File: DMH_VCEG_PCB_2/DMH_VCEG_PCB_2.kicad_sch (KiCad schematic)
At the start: 0 parts

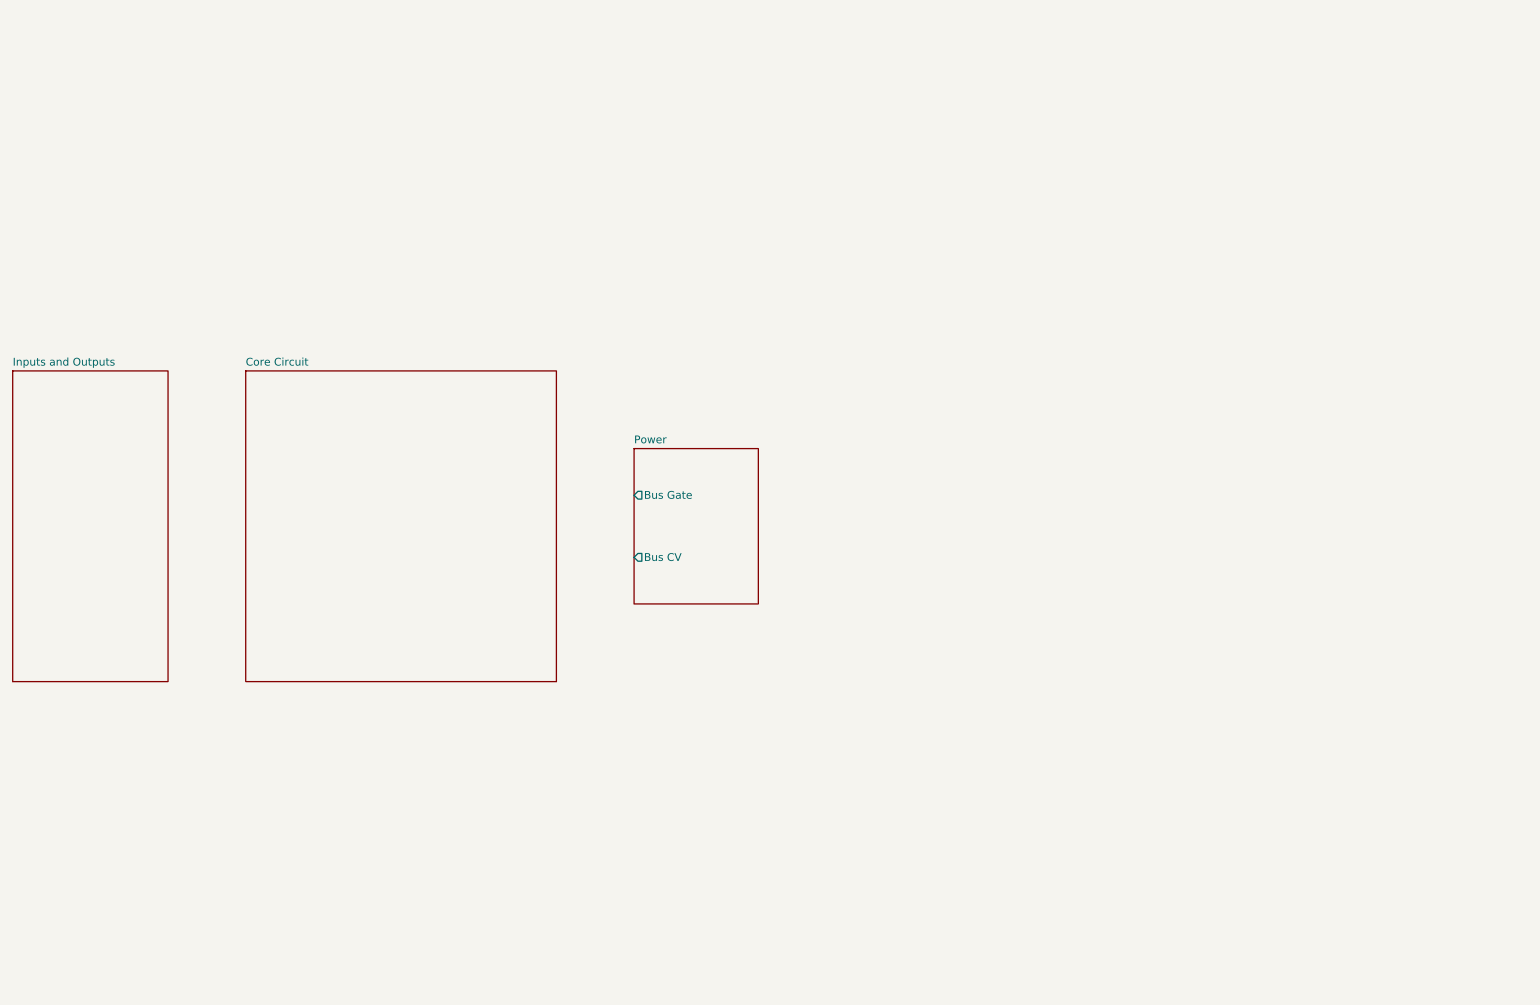
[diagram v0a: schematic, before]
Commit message: Copied PCB 1 as PCB 2
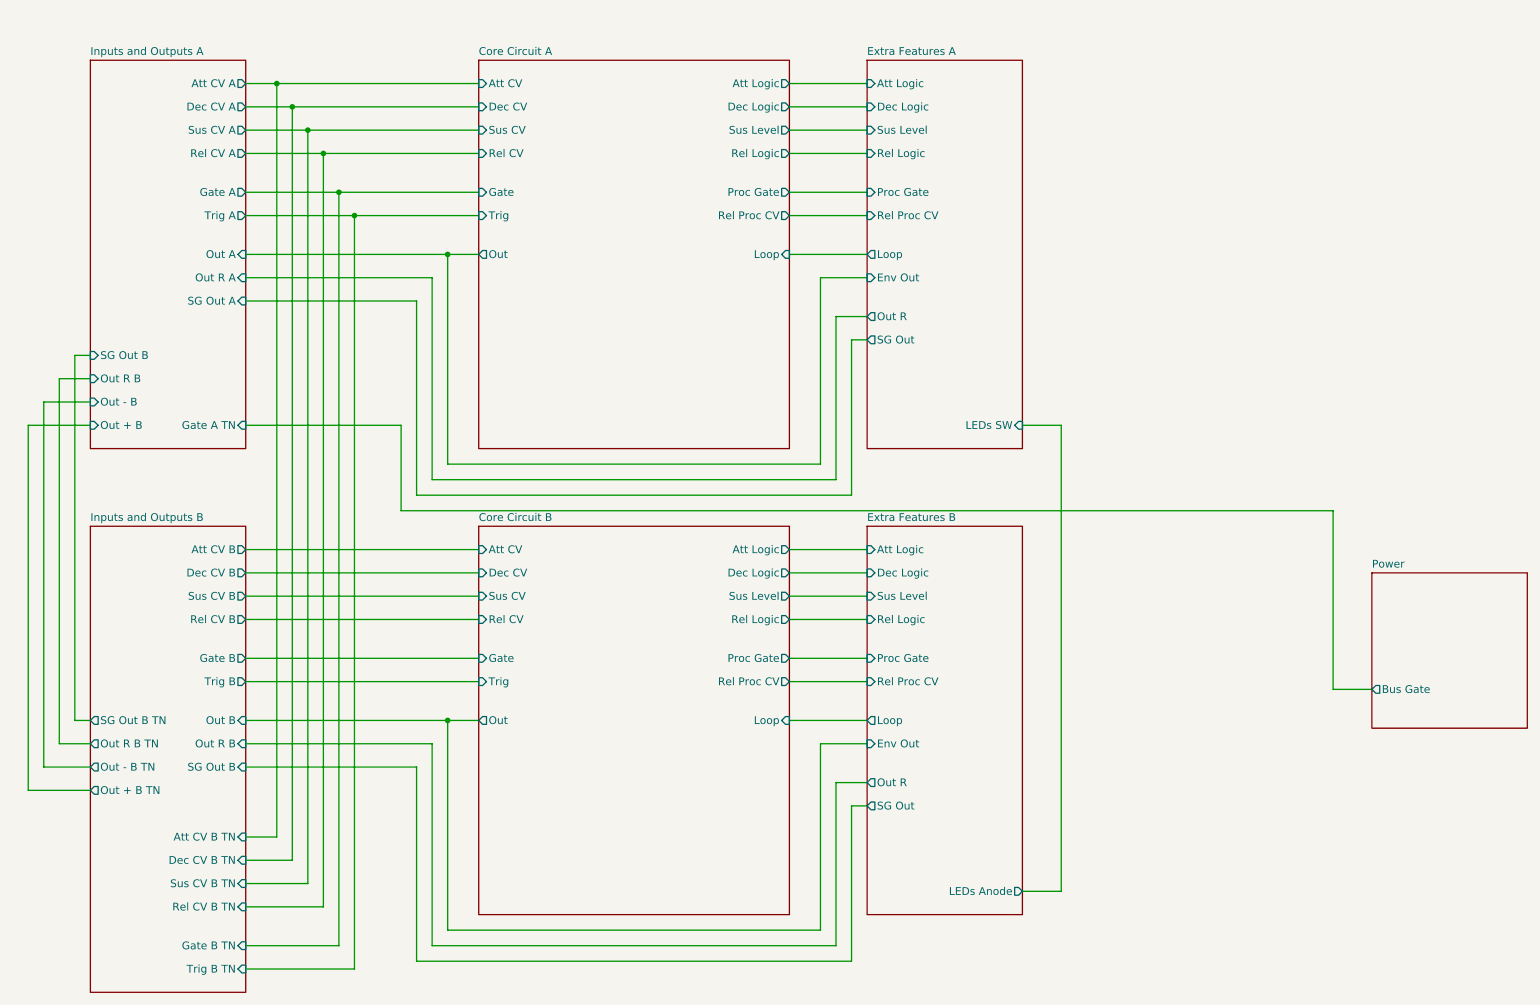
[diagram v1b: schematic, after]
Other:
- sheet Inputs and Outputs renamed Inputs and Outputs A
- removed sheet Core Circuit
- added sheet Core Circuit A (Core_Circuit_A.kicad_sch)
- added sheet Core Circuit B (Core_Circuit_B.kicad_sch)
- added sheet Extra Features A (Extra_Features_A.kicad_sch)
- added sheet Extra Features B (Extra_Features_B.kicad_sch)
- added sheet Inputs and Outputs B (Inputs_and_Outputs_B.kicad_sch)
- sheet Inputs and Outputs A: file Inputs_and_Outputs.kicad_sch -> Inputs_and_Outputs_A.kicad_sch
- sheet Inputs and Outputs A ports: added Att CV A, Dec CV A, Gate A, Gate A TN, Out + B, Out - B, Out A, Out R A, Out R B, Rel CV A, SG Out A, SG Out B, Sus CV A, Trig A; removed none
- sheet Power ports: added none; removed Bus CV

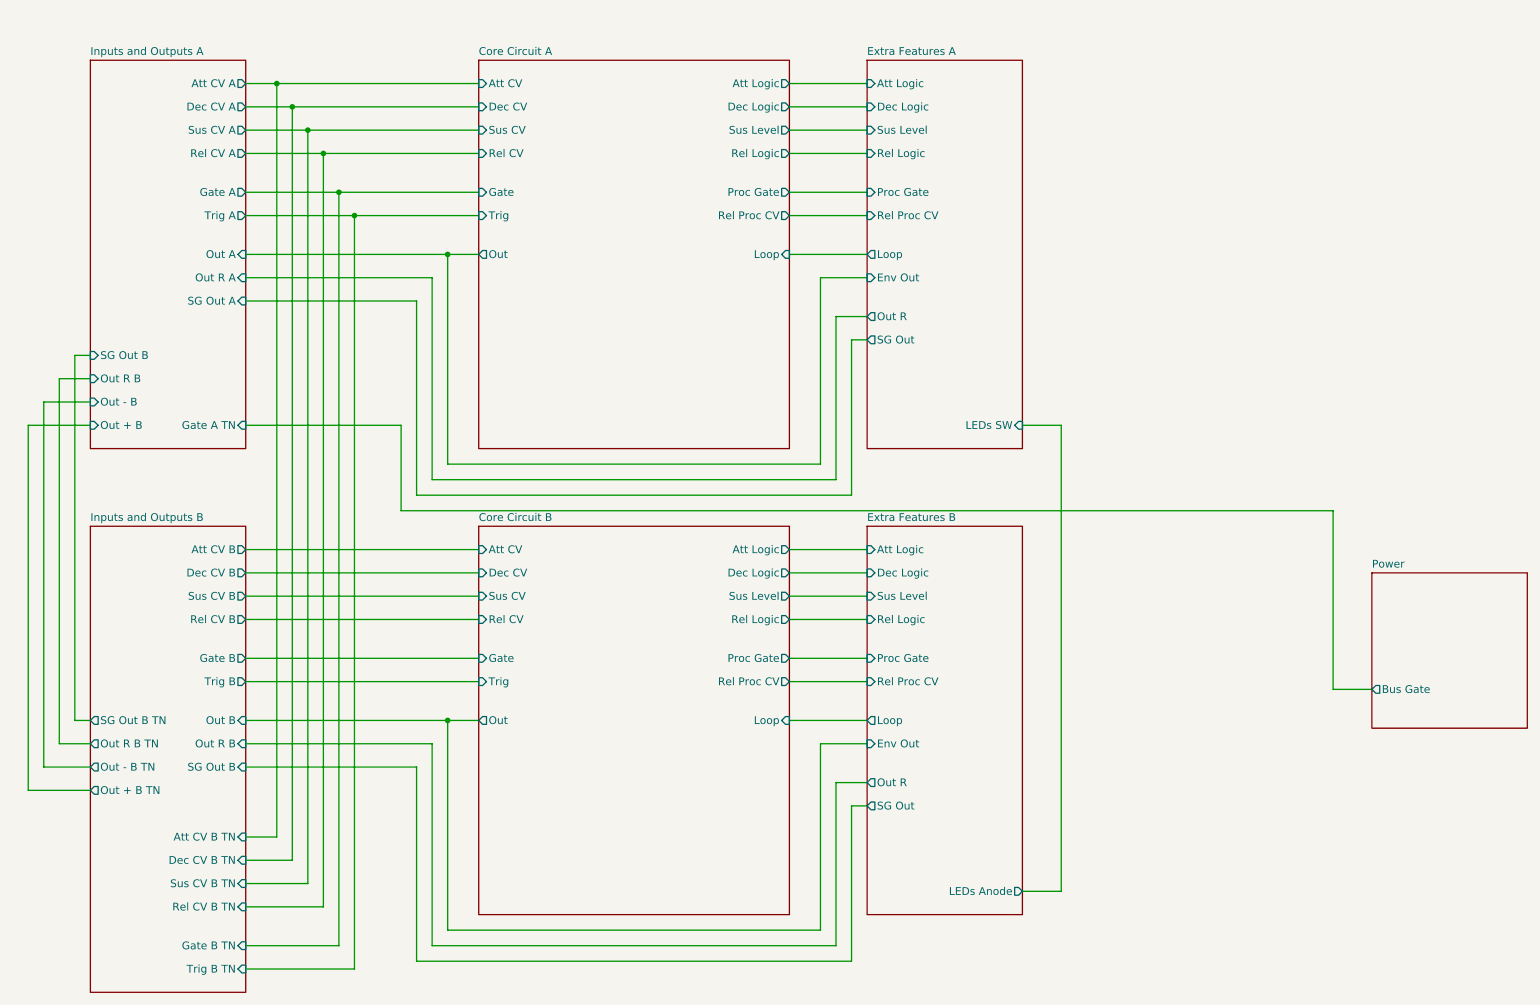
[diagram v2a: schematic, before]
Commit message: Synced PCB 2 project with PCB 1
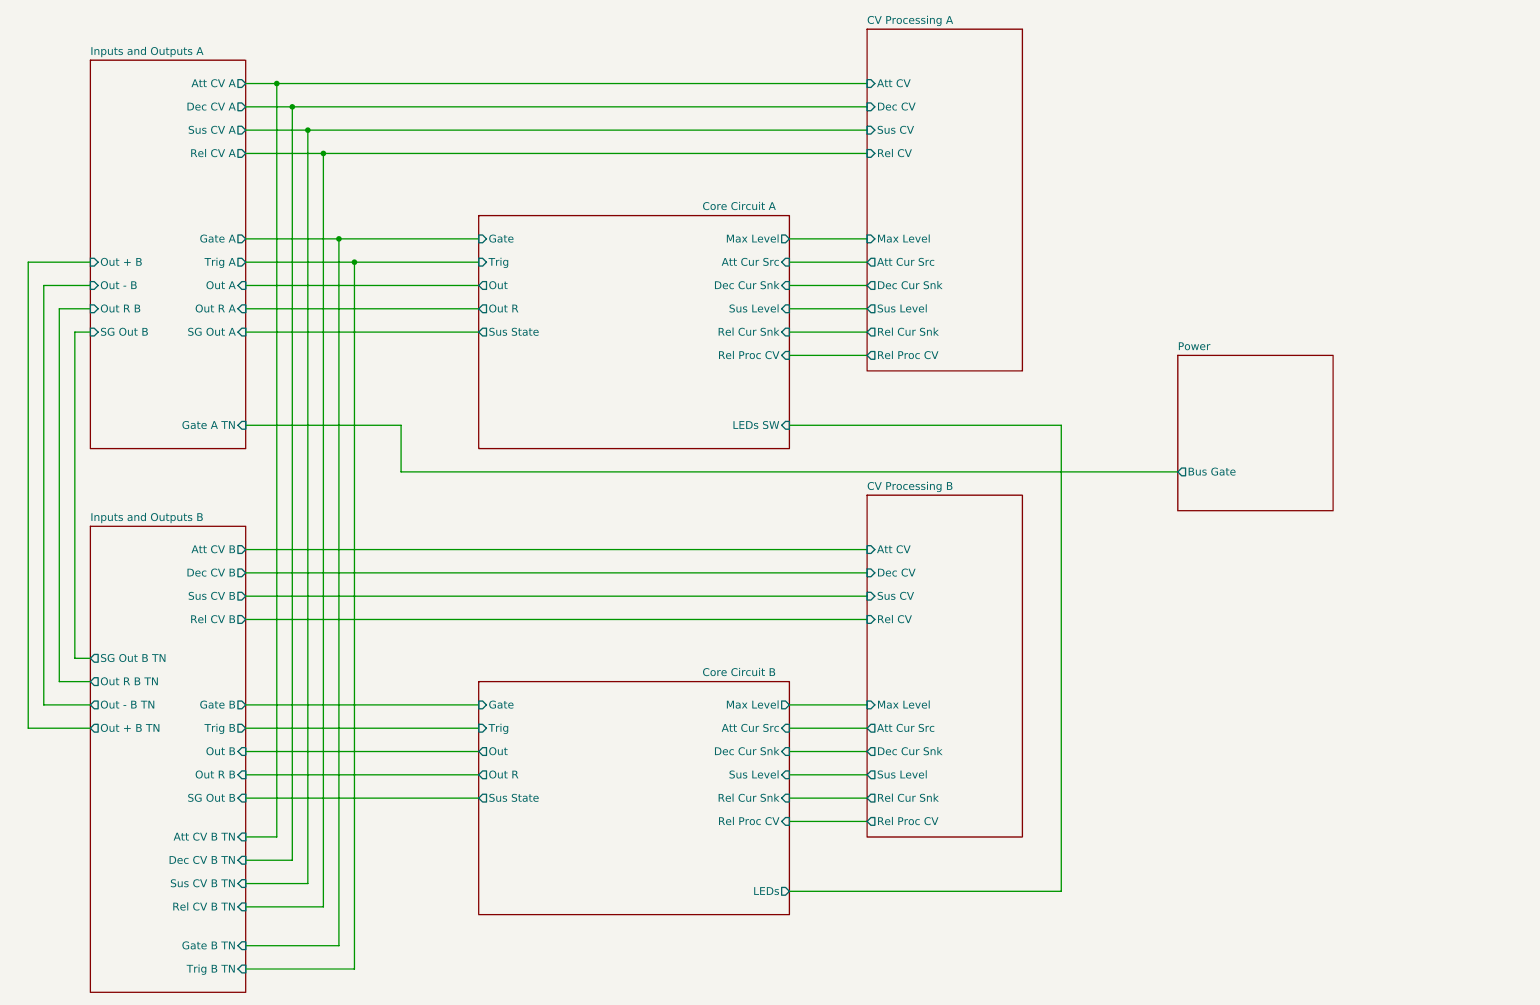
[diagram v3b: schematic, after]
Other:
- removed sheet Extra Features A
- removed sheet Extra Features B
- added sheet CV Processing A (CV_Processing_A.kicad_sch)
- added sheet CV Processing B (CV_Processing_B.kicad_sch)
- sheet Core Circuit A ports: added Att Cur Src, Dec Cur Snk, LEDs SW, Max Level, Out R, Rel Cur Snk, Sus State; removed Att CV, Att Logic, Dec CV, Dec Logic, Loop, Proc Gate, Rel CV, Rel Logic, Sus CV
- sheet Core Circuit B ports: added Att Cur Src, Dec Cur Snk, LEDs, Max Level, Out R, Rel Cur Snk, Sus State; removed Att CV, Att Logic, Dec CV, Dec Logic, Loop, Proc Gate, Rel CV, Rel Logic, Sus CV

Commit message: Synced changes to PCB 2
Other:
- sheet Core Circuit A ports: added Inv Sus State; removed Sus State
- sheet Core Circuit B ports: added Inv Sus State; removed Sus State
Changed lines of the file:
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@@
 			)
 		)
-		(pin "Sus State" output
+		(pin "Inv Sus State" output
 			(at 101.6 146.05 180)
 			(effects
@@
 			)
 		)
-		(pin "Sus State" output
+		(pin "Inv Sus State" output
 			(at 101.6 69.85 180)
 			(effects
